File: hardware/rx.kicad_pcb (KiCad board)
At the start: 2 copper layers, 100 x 80 mm, 137 parts, among them J1 RX-RF, J10 ROT, J11 TxOsc, J13 Conn_Coaxial, J2 HP, J3 AVR-ISP-6, J4 ToPA, J5 Key, J6 Supply, J7 SW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

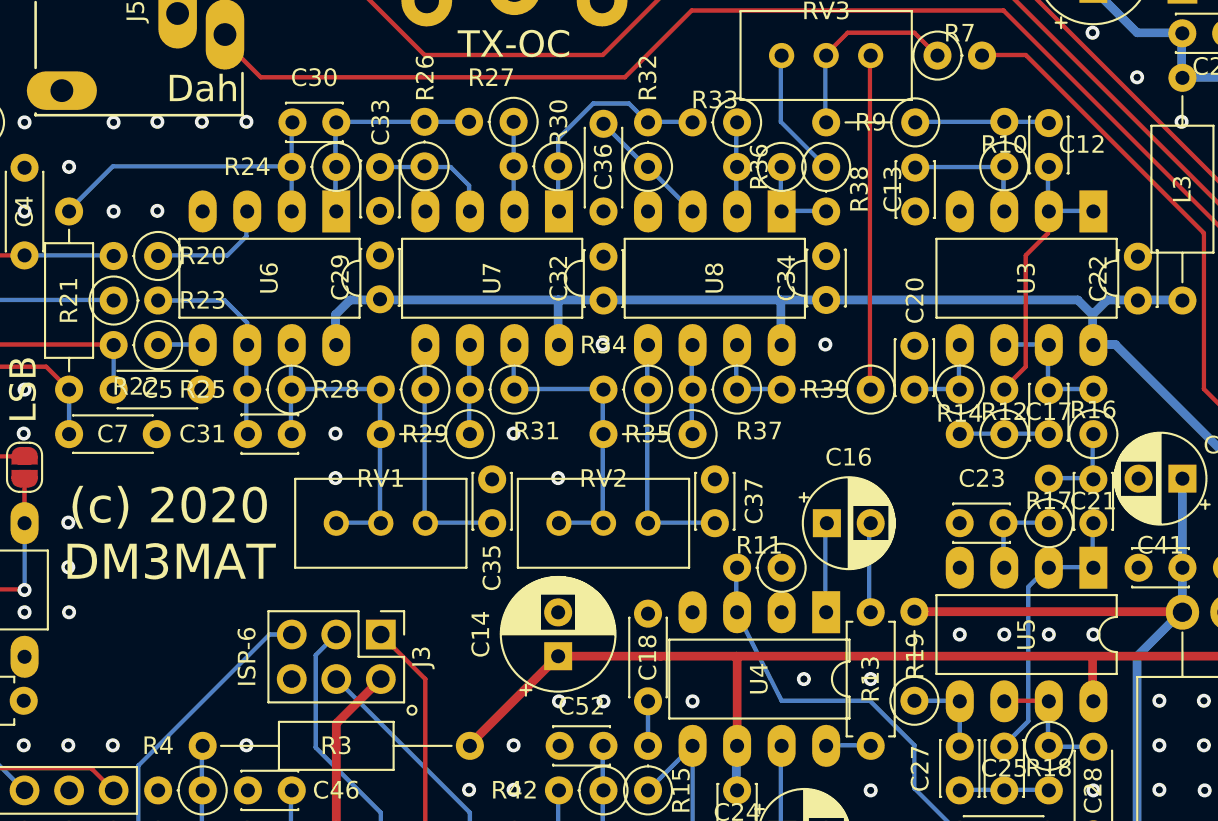
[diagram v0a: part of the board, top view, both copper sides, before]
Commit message: Minor fixes to LP filter.
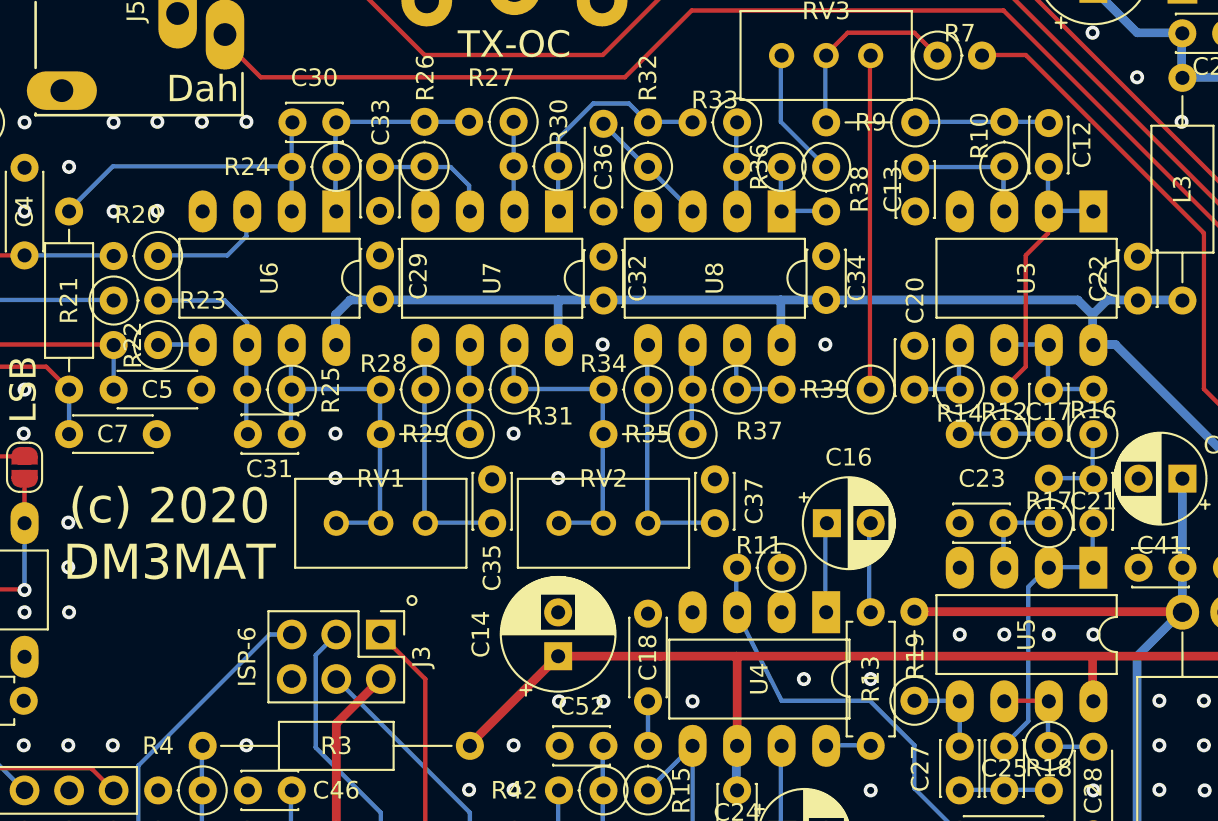
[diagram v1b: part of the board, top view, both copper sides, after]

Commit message: Fixed docs.
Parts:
- U3, U5, U6, U7, U8: value TLC272 -> LM833
